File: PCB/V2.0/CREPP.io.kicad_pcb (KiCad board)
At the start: 2 copper layers, 247.5 x 183.2 mm, 134 parts, among them J1 Screw_Terminal_01x02, J10 Power_Selector, J11 Screw_Terminal_01x02, J12 Screw_Terminal_01x04, J13 Conn_02x04_Odd_Even, J14 OLED_SOCKET, J15 Conn_02x04_Odd_Even, J16 I2C_Selector, J17 Conn_02x04_Odd_Even, J18 Conn_02x04_Odd_Even, J19 Screw_Terminal_01x02, J2 HC-SR04_VIRTUAL, J20 ST_PH_B4B-PH-K_1x04_P2.00mm, J21 Conn_02x04_Odd_Even, J22 OLED_SOCKET_VIRTUAL, J23 HC-SR, J24 BME_VIRTUAL, J25 BME, J26 Servo, J27 SIG_HCSR04, J28 Conn_02x20, J29 Sig_Servo, J3 Conn_02x04_Odd_Even, J30 Servo, J31 ST_PH_B4B-PH-K_1x04_P2.00mm, J32 Power_Servo_Selector, J33 Screw_Terminal_01x02, J34 Sig_Servo, J36 Power_Selector, J4 Conn_01x20, J40 Conn_01x08_Socket, J5 Conn_01x20, J6 Conn_02x20, J7 VIRTUAL_MPU6050, J8 ST_PH_B4B-PH-K_1x04_P2.00mm, J9 ST_PH_B4B-PH-K_1x04_P2.00mm, M1 Motor_DC, M2 Motor_DC, M3 Motor_DC, Q3 2N7002, Q4 IRF520, SW1 SW_Left, SW2 SW_Up, SW3 SW_Right, SW4 SW_Down, SW5 SW_Right, SW6 RotaryEncoder_Switch, SW7 SW_Left, SW8 SW_Right, U1 PC817, U11 PC817, U12 PC817, U2 L293D, U3 NRF24L01_Breakout, U4 DS1302+, U5 74HC04, U6 PC817, U7 PC817, Y2 16MHz

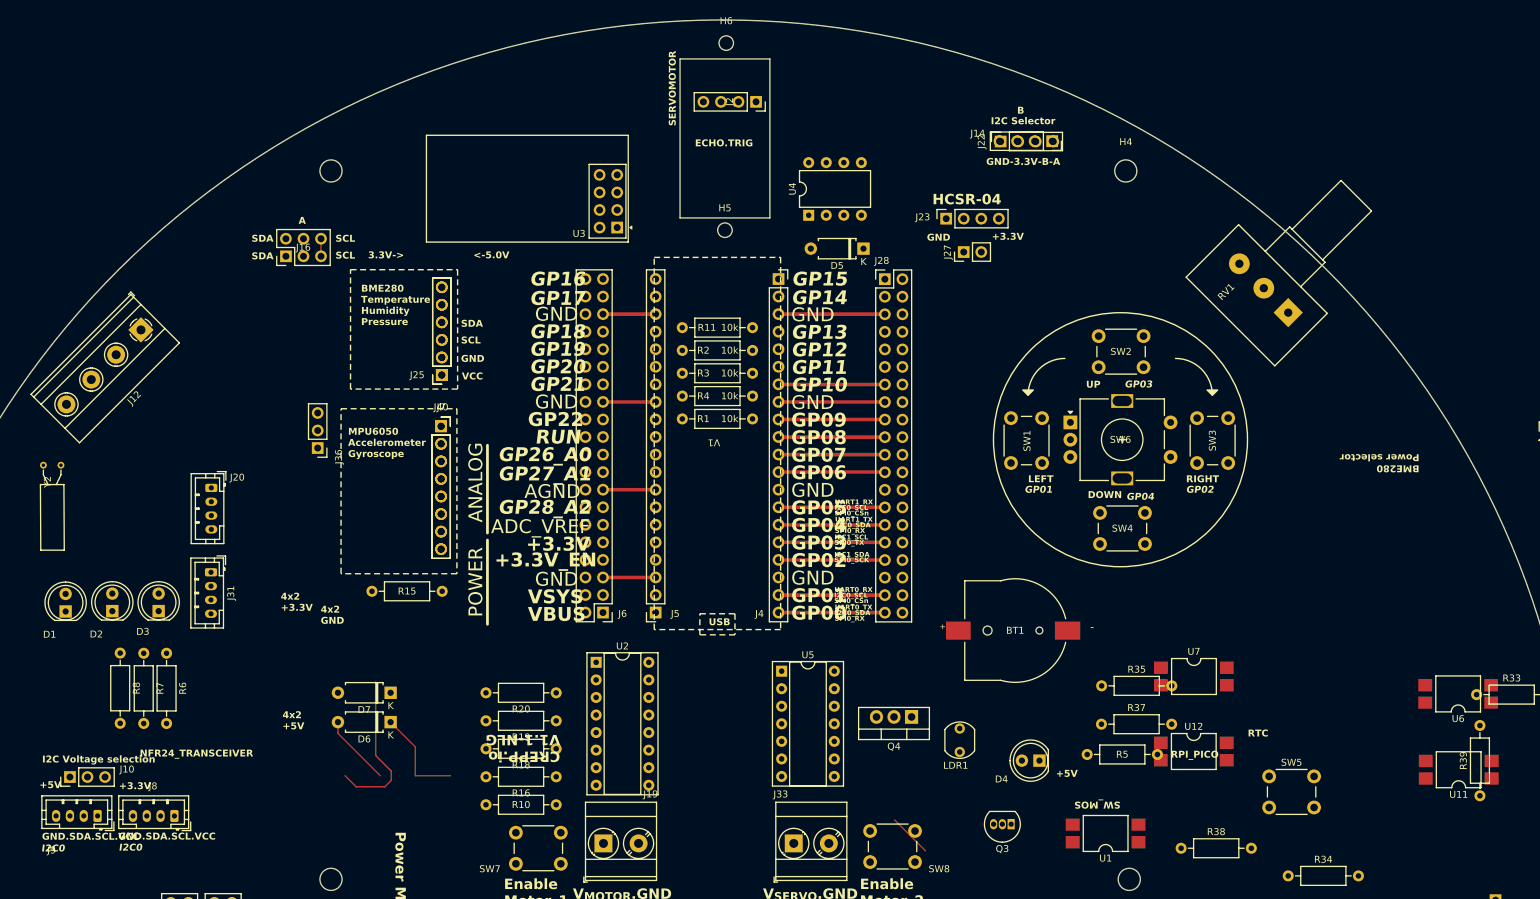
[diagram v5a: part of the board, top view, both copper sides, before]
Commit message: Update of BME and OLED
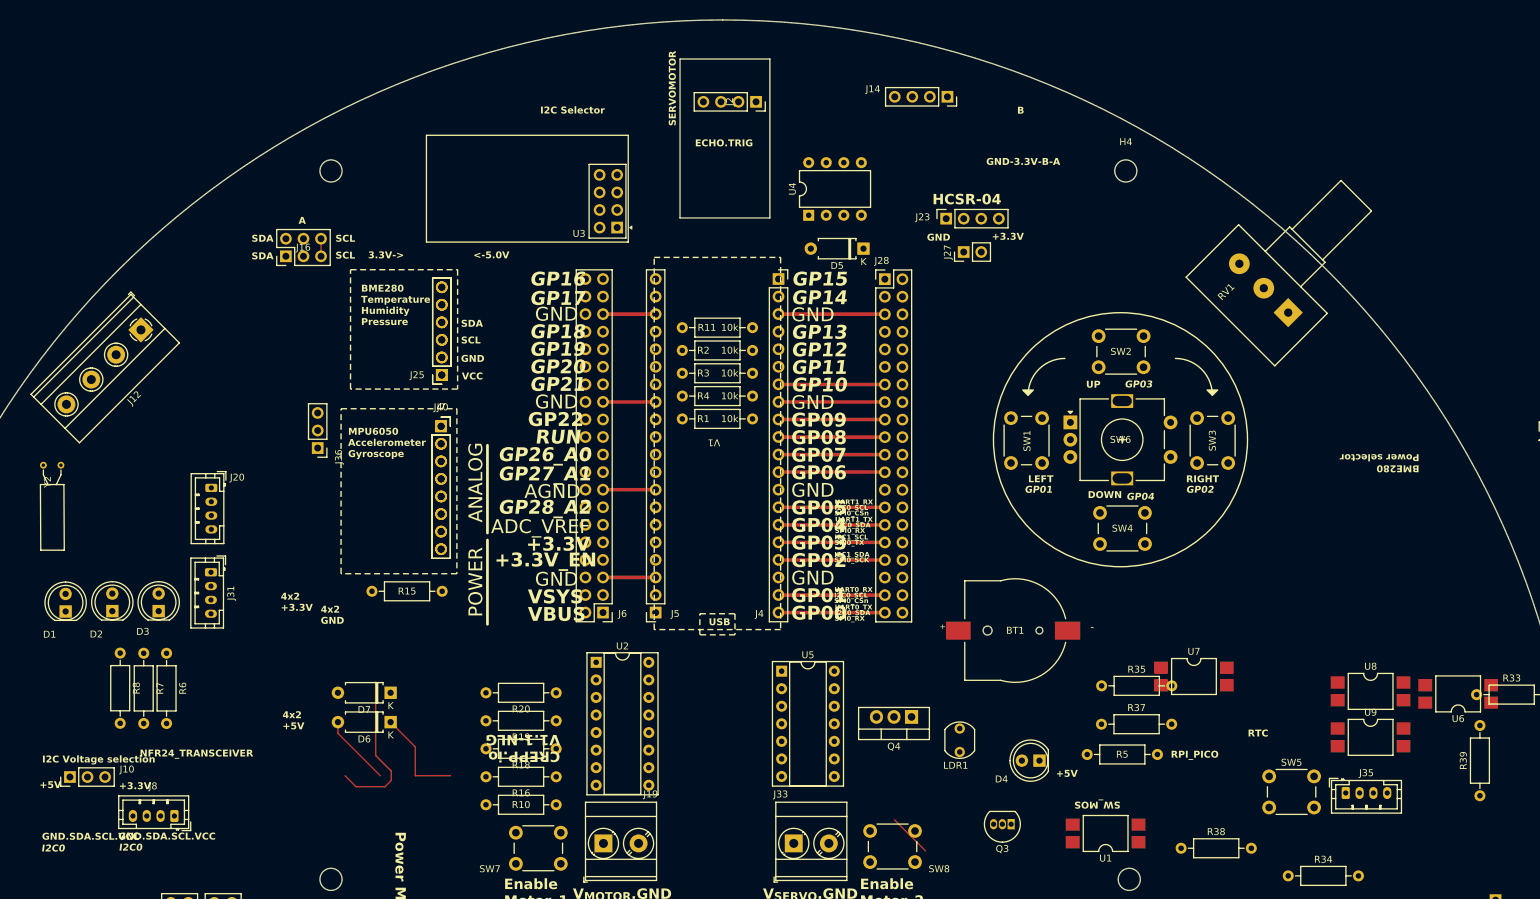
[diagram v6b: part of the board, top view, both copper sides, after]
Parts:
- removed H5, H6: MountingHole, MountingHole:MountingHole_2.1mm
- removed J22: OLED_SOCKET_VIRTUAL, Connector_PinSocket_2.54mm:PinSocket_1x04_P2.54mm_Vertical
- removed J9: ST_PH_B4B-PH-K_1x04_P2.00mm, Connector_JST:JST_PH_B4B-PH-K_1x04_P2.00mm_Vertical
- removed U11, U12: PC817, Package_DIP:SMDIP-4_W9.53mm
- added J35: Coon_01x04_Pin_2mm, Connector_JST:JST_PH_B4B-PH-K_1x04_P2.00mm_Vertical, F.Cu at (264.1, 159.7)
- added JP30: Jumper_2.54mm_red, CREPP_Jumpers:Jumper_2.54mm_red, F.Cu at (278.1, 143.5)
- added OLED1: ~, CREPP_Screens:SSD1306_OLED_Display_VIRTUAL_128_64, F.Cu at (275.6, 201.2)
- added U8: PC817_SMD, Package_DIP:SMDIP-4_W9.53mm, F.Cu at (267.7, 145.0)
- added U9: PC817_SMD, Package_DIP:SMDIP-4_W9.53mm, F.Cu at (267.7, 151.6)
- J8: value ST_PH_B4B-PH-K_1x04_P2.00mm -> Coon_01x04_Pin_2mm
- SW6: footprint Rotary_Encoder:RotaryEncoder_Alps_EC11E-Switch_Vertical_H20mm -> CREPP_RotaryEncoders:RotaryEncoder
- U1, U6, U7: value PC817 -> PC817_SMD
- moved J14 16.5 mm to (206.5, 58.9)

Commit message: update
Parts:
- removed J24: BME_VIRTUAL, Connector_PinSocket_2.54mm:PinSocket_1x06_P2.54mm_Vertical
- added U10: ~, CREPP_Temperature_sensors:BME280_Breakout, F.Cu at (125.0, 92.8)
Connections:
- SW6 pad A: unconnected-(SW6-PadA) -> /UserActions/DT
- SW6 pad B: unconnected-(SW6-PadB) -> /UserActions/CLK
- SW6 pad C: unconnected-(SW6-PadC) -> GND

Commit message: Update board
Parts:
- removed J10: Power_Selector, Connector_PinHeader_2.54mm:PinHeader_1x03_P2.54mm_Vertical
- removed J20, J31: ST_PH_B4B-PH-K_1x04_P2.00mm, Connector_JST:JST_PH_B4B-PH-K_1x04_P2.00mm_Vertical
- removed J35: Coon_01x04_Pin_2mm, Connector_JST:JST_PH_B4B-PH-K_1x04_P2.00mm_Vertical
- removed M3: Motor_DC, Connector_PinHeader_2.54mm:PinHeader_1x01_P2.54mm_Vertical
- removed Y2: 16MHz, Crystal:Crystal_AT310_D3.0mm_L10.0mm_Horizontal
- added D8: LED, LED_THT:LED_D5.0mm, F.Cu at (253.1, 137.3)
- added J9: Coon_01x04_Pin_2mm, Connector_JST:JST_PH_B4B-PH-K_1x04_P2.00mm_Vertical, F.Cu at (77.8, 162.1)
- added R9: 270, Resistor_THT:R_Axial_DIN0207_L6.3mm_D2.5mm_P10.16mm_Horizontal, F.Cu at (252.2, 131.6)
- added SW9: SW_Left, Button_Switch_THT:SW_PUSH_6mm, F.Cu at (205.9, 89.3)
- BT1: footprint BC501SM:MPD_BC501SM-TR -> CREPP_Batteries_holders:MPD_BC501SM-TR
- U4: value DS1302+ -> DS3231M; footprint Package_DIP:DIP-8_W7.62mm -> Package_SO:SOIC-16W_7.5x10.3mm_P1.27mm
- moved U4 50.7 mm to (208.3, 121.8), turned to 180 degrees
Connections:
- net /LDR renamed /MCU/GP27
- net /MOSFET/GND renamed GND_MOS
- net /MOSFET/MOSFET renamed /MCU/GP17
- net /Motors/GND_Power renamed GND_POWER
- net /POT renamed /MCU/GP26
- net /Power/Ext_Servo renamed /Servo_Power/Ext_Servo
- D5 pad 2: /Motors/+V_Control -> +5V
- J12 pad 4: /MOSFET/GND_Power -> GND
- J13 pad 2: /MCU/SCL -> /I2C_Interface/SCL
- J13 pad 4: /MCU/SCL -> /I2C_Interface/SCL
- J13 pad 6: /MCU/SCL -> /I2C_Interface/SCL
- J13 pad 8: /MCU/SCL -> /I2C_Interface/SCL
- J15 pad 1: /MCU/SDA -> /I2C_Interface/SDA
- J15 pad 2: /MCU/+3.3V -> +3.3V
- J15 pad 3: /MCU/SDA -> /I2C_Interface/SDA
- J15 pad 4: /MCU/+3.3V -> +3.3V
- J15 pad 5: /MCU/SDA -> /I2C_Interface/SDA
- J15 pad 6: /MCU/+3.3V -> +3.3V
- J15 pad 7: /MCU/SDA -> /I2C_Interface/SDA
- J15 pad 8: /MCU/+3.3V -> +3.3V
- J16 pad 1: /OLED/SDA -> /I2C_Interface/SDA
- J16 pad 2: /OLED/SDA -> /I2C_Interface/SDA
- J16 pad 5: /OLED/SCL -> /I2C_Interface/SCL
- J16 pad 6: /OLED/SCL -> /I2C_Interface/SCL
- J25 pad 3: /OLED/SDA -> /I2C_Interface/SDA
- J25 pad 4: /OLED/SCL -> /I2C_Interface/SCL
- J28 pad 20: /MCU/GP8 -> /LED/GREEN
- J28 pad 22: /MCU/GP7 -> /LED/ORANGE_LED
- J28 pad 24: /MCU/GP6 -> /LED/RED_LED
- J28 pad 28: /MCU/GP5 -> /I2C_Interface/SCL
- J28 pad 30: /MCU/GP4 -> /I2C_Interface/SDA
- J40 pad 3: /IMU/SDA -> /I2C_Interface/SDA
- J40 pad 4: /IMU/SCL -> /I2C_Interface/SCL
- J5 pad 1: unconnected-(J5-Pin_1-Pad1) -> Net-(J5-Pin_1)
- J5 pad 11: Net-(J5-Pin_11) -> /MCU/RUN
- J5 pad 2: unconnected-(J5-Pin_2-Pad2) -> Net-(J5-Pin_2)
- J5 pad 4: unconnected-(J5-Pin_4-Pad4) -> Net-(J5-Pin_4)
- J5 pad 5: unconnected-(J5-Pin_5-Pad5) -> Net-(J5-Pin_5)
- J5 pad 6: unconnected-(J5-Pin_6-Pad6) -> Net-(J5-Pin_6)
- J6 pad 1: unconnected-(J6-Pin_1-Pad1) -> Net-(J5-Pin_1)
- J6 pad 10: unconnected-(J6-Pin_10-Pad10) -> +3.3V
- J6 pad 11: unconnected-(J6-Pin_11-Pad11) -> Net-(J5-Pin_6)
- J6 pad 16: unconnected-(J6-Pin_16-Pad16) -> /MCU/GND
- J6 pad 2: unconnected-(J6-Pin_2-Pad2) -> +5V
- J6 pad 21: Net-(J5-Pin_11) -> /MCU/RUN
- J6 pad 22: unconnected-(J6-Pin_22-Pad22) -> /MCU/RUN
- J6 pad 24: unconnected-(J6-Pin_24-Pad24) -> /MCU/GP22
- J6 pad 26: unconnected-(J6-Pin_26-Pad26) -> /MCU/GND
- J6 pad 28: unconnected-(J6-Pin_28-Pad28) -> /MCU/GP21
- J6 pad 3: unconnected-(J6-Pin_3-Pad3) -> Net-(J5-Pin_2)
- J6 pad 30: unconnected-(J6-Pin_30-Pad30) -> /MCU/GP20
- J6 pad 4: unconnected-(J6-Pin_4-Pad4) -> /MCU/V_{SYS}
- J6 pad 6: unconnected-(J6-Pin_6-Pad6) -> /MCU/GND
- J6 pad 7: unconnected-(J6-Pin_7-Pad7) -> Net-(J5-Pin_4)
- J6 pad 9: unconnected-(J6-Pin_9-Pad9) -> Net-(J5-Pin_5)
- J8 pad 1: /I2C_Interface/VCC_Common -> GND
- J8 pad 2: /I2C_Interface/SCL -> /I2C_Interface/SDA
- J8 pad 3: /I2C_Interface/SDA -> /I2C_Interface/SCL
- J8 pad 4: /I2C_Interface/GND -> +3.3V
- Q4 pad 3: /MOSFET/GND_Power -> GND
- R1 pad 1: /UserActions/PB_LEFT -> /MCU/GP11
- R10 pad 2: /MOSFET/+3.3V -> +3.3V
- R11 pad 1: /UserActions/PB_DOWN -> /MCU/GP13
- R18 pad 2: /MOSFET/+3.3V -> +3.3V
- R2 pad 1: /UserActions/PB_UP -> /MCU/GP9
- R20 pad 2: /MOSFET/GND_Power -> GND
- R3 pad 1: /UserActions/PB_RIGHT -> /MCU/GP12
- R33 pad 2: /Motors/DIR_M1 -> /MCU/GP0
- R35 pad 2: /Motors/EN_M1 -> /MCU/GP1
- R37 pad 2: /Motors/EN_M2 -> /MCU/GP3
- R39 pad 2: /Motors/DIR_M2 -> /MCU/GP2
- R4 pad 1: /UserActions/PB_DOWN -> /MCU/GP10
- RV1 pad 1: GND -> +3.3V
- RV1 pad 3: +3.3V -> GND
- SW1 pad 2: /UserActions/PB_LEFT -> /MCU/GP11
- SW2 pad 2: /UserActions/PB_UP -> /MCU/GP9
- SW3 pad 2: /UserActions/PB_RIGHT -> /MCU/GP12
- SW4 pad 2: /UserActions/PB_DOWN -> /MCU/GP10
- SW5 pad 2: /Motors/L239D_Interfaces/GND -> GND
- SW6 pad A: /UserActions/DT -> /MCU/GP14
- SW6 pad B: /UserActions/CLK -> /MCU/GP15
- SW6 pad S1: /UserActions/PB_DOWN -> /MCU/GP13
- SW8 pad 2: /Motors/L239D_Interfaces/GND -> GND
- U1 pad 3: /MOSFET/GND_Power -> GND
- U3 pad 1: /NRF24/GND -> GND
- U3 pad 2: /NRF24/+3.3V -> +3.3V
- U3 pad 3: /NRF24/CE -> /MCU/GP21
- U3 pad 4: /NRF24/~{CSN} -> /MCU/GP20
- U3 pad 5: /NRF24/SCK -> /MCU/GP18
- U3 pad 6: /NRF24/MOSI -> /MCU/GP19
- U3 pad 7: /NRF24/MISO -> /MCU/GP16
- U4 pad 1: +3.3V -> unconnected-(U4-32KHZ-Pad1)
- U4 pad 2: Net-(U4-X1) -> +3.3V
- U4 pad 4: GND -> +3.3V
- U4 pad 5: /RTC/CE -> GND
- U4 pad 6: /RTC/MOSI -> GND
- U4 pad 7: /RTC/SCK -> GND
- U4 pad 8: Net-(BT1-+) -> GND
- U6 pad 2: /Motors/L239D_Interfaces/GND -> GND
- U6 pad 3: /Motors/L239D_Interfaces/GND -> GND
- U7 pad 2: /Motors/L239D_Interfaces/GND -> GND
- U7 pad 3: /Motors/L239D_Interfaces/GND -> GND
- U8 pad 2: /Motors/L239D_Interfaces/GND -> GND
- U8 pad 3: /Motors/L239D_Interfaces/GND -> GND
- U9 pad 2: /Motors/L239D_Interfaces/GND -> GND
- U9 pad 3: /Motors/L239D_Interfaces/GND -> GND
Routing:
- net /MOSFET/GND_Power: track 22.9 -> 0.00 mm
- net (no net): track 0.00 -> 22.9 mm
- net GND: track 0.00 -> 6.33 mm
- net /Motors/L239D_Interfaces/GND: track 6.33 -> 0.00 mm
- net /OLED/SCL: track 2.54 -> 0.00 mm
- net /I2C_Interface/SCL: track 0.00 -> 2.54 mm
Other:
- board text added: "SPI0_MISO"
- board text added: "SPI0_MOSI"
- board text removed: "SPI0_TX"
